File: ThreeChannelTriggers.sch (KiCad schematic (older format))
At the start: 105 parts, among them SW1 SW_SPST, SW10 SW_SPST, SW11 SW_SPST, SW12 SW_SPST, SW13 SW_SPST, SW14 SW_SPST, SW15 SW_SPST, SW16 SW_SPST, SW17 SW_SPST, SW18 SW_SPST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

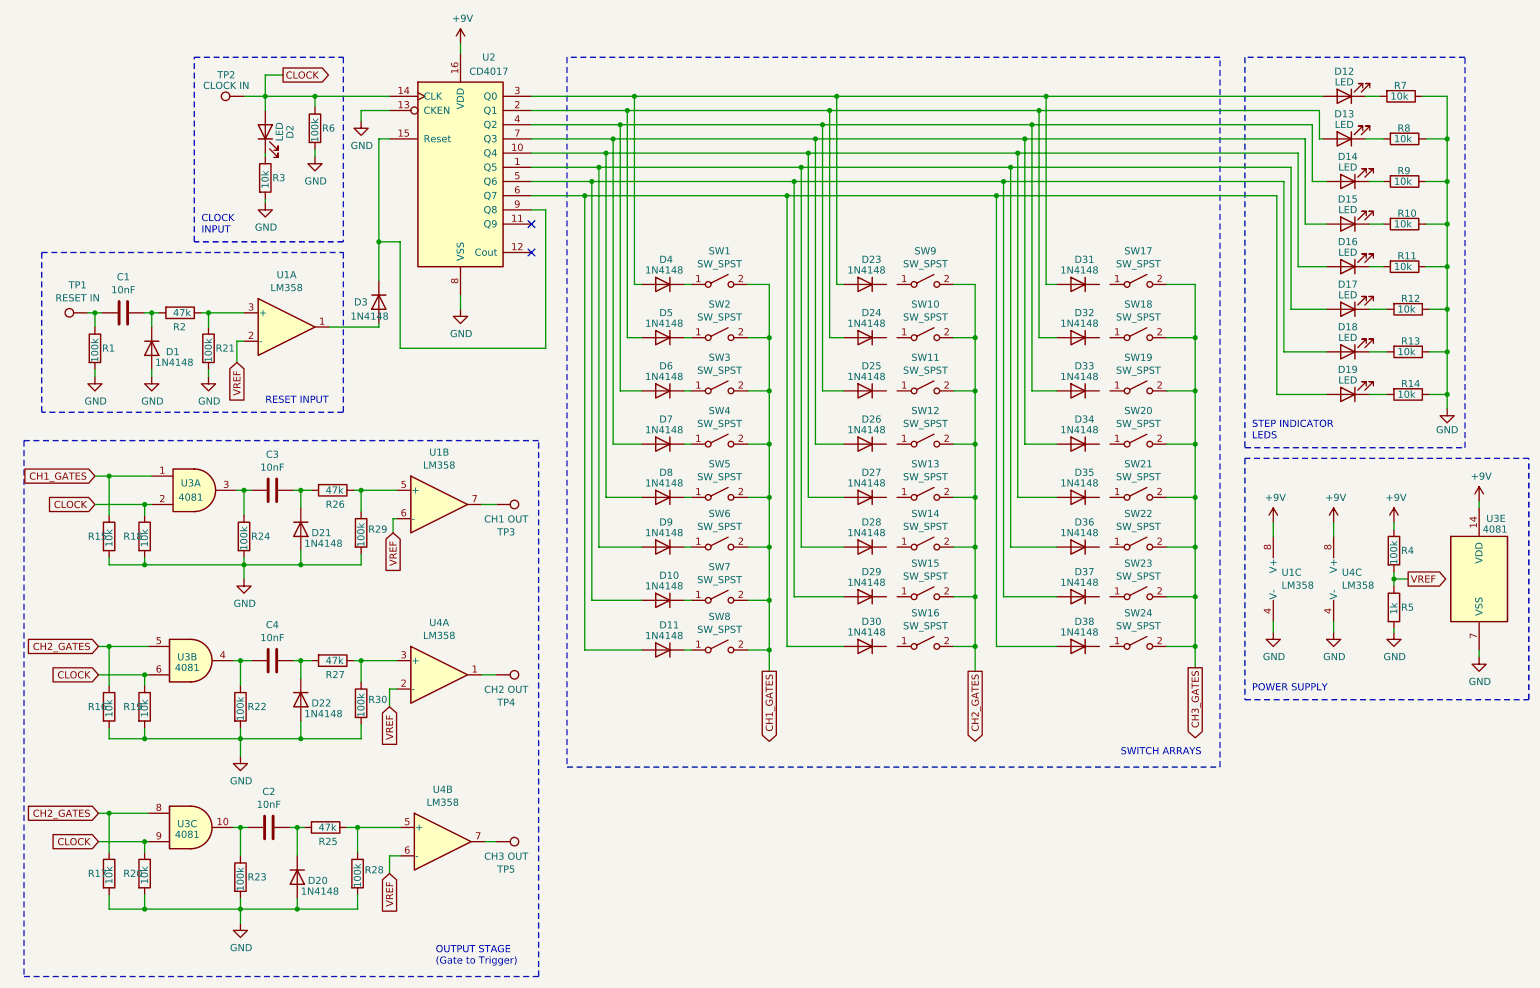
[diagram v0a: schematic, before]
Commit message: Fixed Channel 3 label
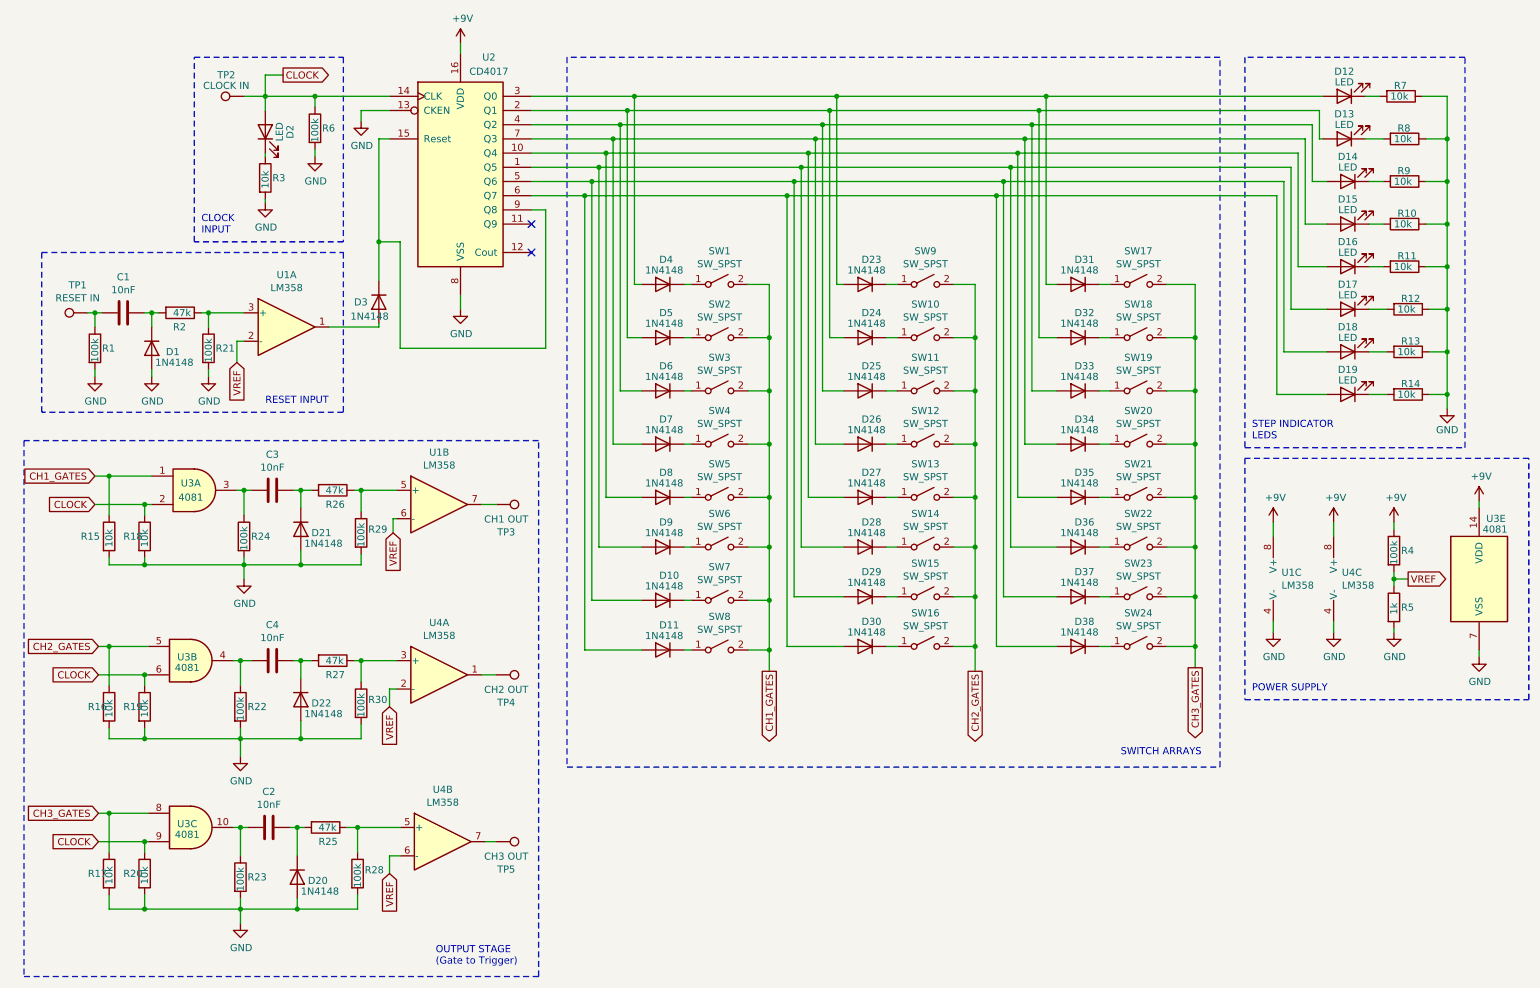
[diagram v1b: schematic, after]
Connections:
- net CH2_GATES: no longer R17.1, U3.8
- net CH3_GATES: now also R17.1, U3.8
- net at D23.1 (K): now also SW9.1 (A)
- net at D24.1 (K): now also SW10.1 (A)
- net at D25.1 (K): now also SW11.1 (A)
- net at D26.1 (K): now also SW12.1 (A)
- net at D27.1 (K): now also SW13.1 (A)
- net at D28.1 (K): now also SW14.1 (A)
- net at D29.1 (K): now also SW15.1 (A)
- net at D30.1 (K): now also SW16.1 (A)
- net at D31.1 (K): now also SW17.1 (A)
- net at D32.1 (K): now also SW18.1 (A)
- net at D33.1 (K): now also SW19.1 (A)
- net at D34.1 (K): now also SW20.1 (A)
- net at D35.1 (K): now also SW21.1 (A)
- net at D36.1 (K): now also SW22.1 (A)
- net at D37.1 (K): now also SW23.1 (A)
- net at D38.1 (K): now also SW24.1 (A)
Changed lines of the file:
@@
 U 1 1 616D3FF3
 P 1150 4300
-F 0 "R15" H 1000 4300 50  0000 L CNN
+F 0 "R15" H 950 4300 50  0000 L CNN
 F 1 "10k" V 1150 4225 50  0000 L CNN
 F 2 "" V 1080 4300 50  0001 C CNN
@@
 $EndComp
 Text GLabel 1075 6250 0    50   Input ~ 0
-CH2_GATES
+CH3_GATES
 Text GLabel 1075 6450 0    50   Input ~ 0
 CLOCK
@@
 Wire Notes Line
 	10700 3675 10700 925
+Wire Wire Line
+	6625 2525 6700 2525
+Wire Wire Line
+	8125 2525 8200 2525
+Wire Wire Line
+	8200 2900 8125 2900
+Wire Wire Line
+	8125 3275 8200 3275
+Wire Wire Line
+	8200 3650 8125 3650
+Wire Wire Line
+	8125 4025 8200 4025
+Wire Wire Line
+	8125 4375 8200 4375
+Wire Wire Line
+	8200 4725 8125 4725
+Wire Wire Line
+	8125 5075 8200 5075
+Wire Wire Line
+	6625 5075 6700 5075
+Wire Wire Line
+	6700 4725 6625 4725
+Wire Wire Line
+	6625 4375 6700 4375
+Wire Wire Line
+	6700 4025 6625 4025
+Wire Wire Line
+	6625 3650 6700 3650
+Wire Wire Line
+	6625 3275 6700 3275
+Wire Wire Line
+	6625 2900 6700 2900
 $EndSCHEMATC
